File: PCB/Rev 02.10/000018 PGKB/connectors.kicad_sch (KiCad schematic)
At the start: 3 parts, among them J2 BM04B-SRSS-TB

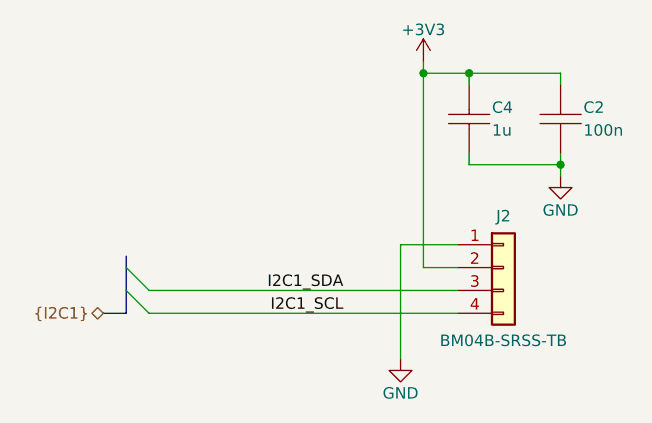
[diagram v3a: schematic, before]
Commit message: Resolved DRC problems
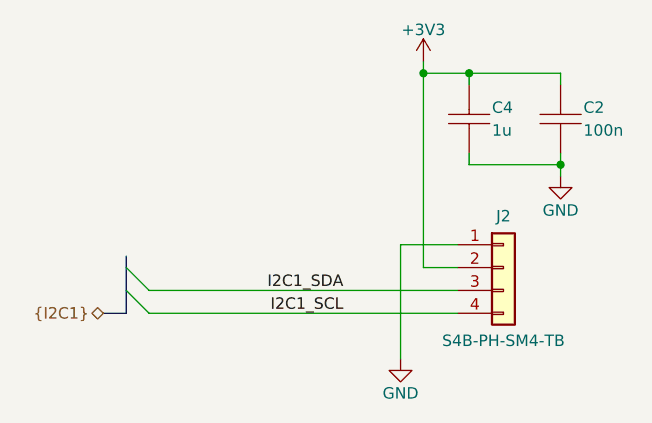
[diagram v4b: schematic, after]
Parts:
- C4: Code 1u -> (none)
- J2: value BM04B-SRSS-TB -> S4B-PH-SM4-TB
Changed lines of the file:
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@@
 			)
 		)
-		(property "Description" ""
+		(property "Description" "Power symbol creates a global label with name \"GND\" , ground"
 			(at 167.64 92.71 0)
 			(effects
@@
 			)
 		)
-		(property "Description" ""
+		(property "Description" "Power symbol creates a global label with name \"GND\" , ground"
 			(at 149.86 113.03 0)
 			(effects
@@
 			)
 		)
-		(property "Value" "BM04B-SRSS-TB"
+		(property "Value" "S4B-PH-SM4-TB"
 			(at 161.29 110.998 0)
 			(do_not_autoplace yes)
@@
 			)
 		)
-		(property "Description" ""
-			(at 156.21 100.33 0)
-			(effects
-				(font
-					(size 1.27 1.27)
-				)
+		(property "Description" "CONN HEADER SMD 4POS 2MM"
+			(at 143.51 68.58 0)
+			(effects
+				(font
+					(size 1.27 1.27)
+				)
+				(justify left)
 				(hide yes)
 			)
@@
 		)
 		(pin "4"
+		)
+		(pin "MP1"
+		)
+		(pin "MP2"
 		)
 		(instances
@@
 		)
 		(property "Value" "1u"
-			(at 144.78 54.61 0)
-			(effects
-				(font
-					(size 1.27 1.27)
-				)
-				(justify left)
-				(hide yes)
+			(at 160.02 87.63 0)
+			(effects
+				(font
+					(size 1.27 1.27)
+				)
+				(justify left)
 			)
 		)
@@
 			)
 		)
-		(property "Description" ""
-			(at 157.48 86.36 0)
-			(effects
-				(font
-					(size 1.27 1.27)
-				)
-				(hide yes)
-			)
-		)
-		(property "Code" "1u"
-			(at 160.02 87.63 0)
-			(effects
-				(font
-					(size 1.27 1.27)
-				)
-				(justify left)
+		(property "Description" "CAP CER 1UF 25V X7R 0805"
+			(at 144.78 54.61 0)
+			(effects
+				(font
+					(size 1.27 1.27)
+				)
+				(justify left)
+				(hide yes)
 			)
 		)
@@
 			)
 		)
-		(property "Description" ""
+		(property "Description" "Power symbol creates a global label with name \"+3V3\""
 			(at 152.4 80.01 0)
 			(effects
@@
 			)
 		)
-		(property "Description" ""
+		(property "Description" "CAP CER 0.1UF 50V X7R 0603"
 			(at 167.64 86.36 0)
 			(effects
